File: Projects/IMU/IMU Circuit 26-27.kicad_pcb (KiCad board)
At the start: 2 copper layers, 55 x 75 mm, 20 parts, among them J1 Conn_02x03_Counter_Clockwise, U1 TJA1050DRG, U2 MCP2515-I, U3 TM171, X1 8MHz

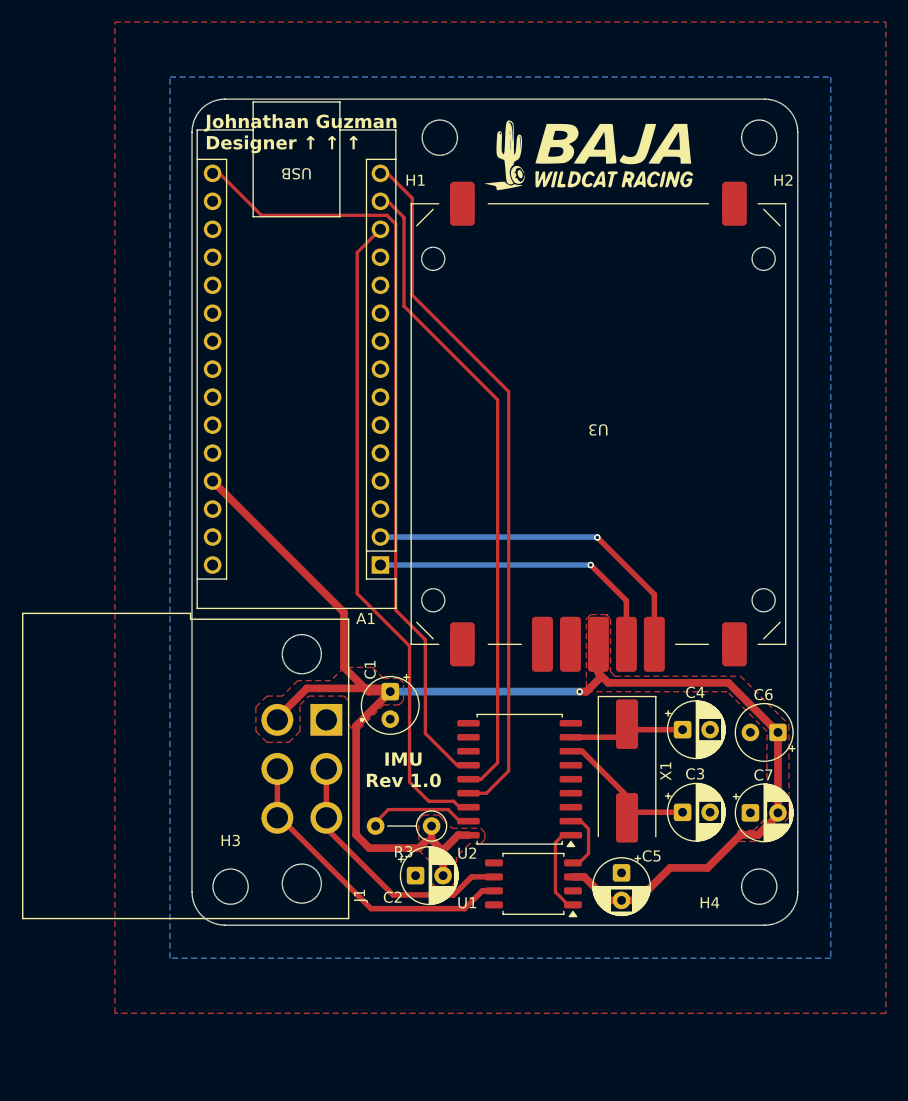
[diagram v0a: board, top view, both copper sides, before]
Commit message: connected int for can controller
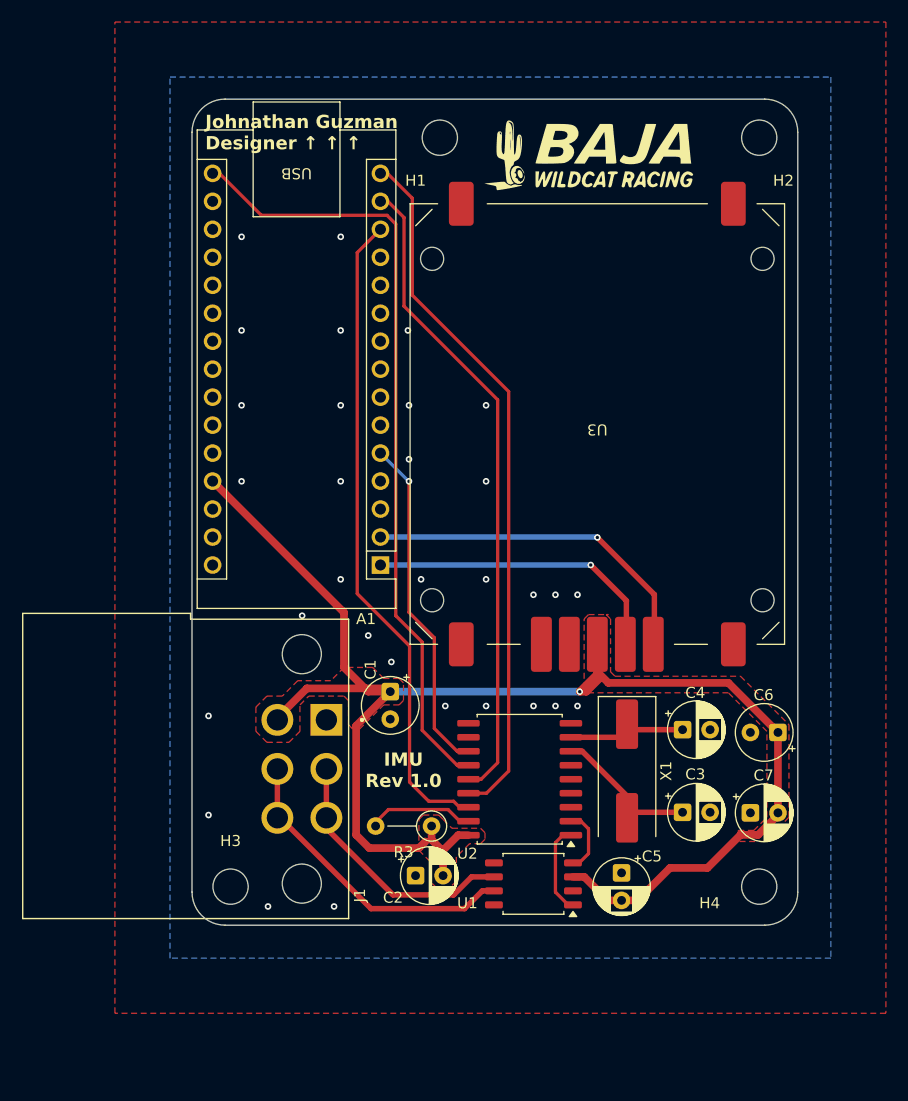
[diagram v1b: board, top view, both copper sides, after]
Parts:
- moved U3 0.10 mm to (138.8, 106.5)
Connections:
- A1 pad 5: unconnected-(A1-D2-Pad5) -> INT
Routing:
- net INT: track 0.00 -> 31.0 mm, vias 0 -> 1
- net +5V: track 138.6 -> 143.5 mm
- net 0: vias 0 -> 31

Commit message: moved some mounting holes
one hole no longer under DTF conn
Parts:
- J1: value Conn_02x03_Counter_Clockwise -> DTF Connector
- moved H3 7.00 mm to (105.5, 155.5)
- moved H4 7.00 mm to (153.5, 155.5)
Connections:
- net 0 renamed GND
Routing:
- net GND: vias 31 -> 29
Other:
- board size 55 x 75 mm -> 55 x 82 mm
- board text added: "BAJA IMU Board Rev 1.0 Designer: Johnathan Guzman"
- board text removed: "IMU Rev 1.0"
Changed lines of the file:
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@@
 			(layers "*.Cu" "*.Mask")
 			(remove_unused_layers no)
-			(net "0")
+			(net "GND")
 			(pinfunction "2_2")
 			(pintype "passive")
@@
 			(layers "F.Cu" "F.Mask" "F.Paste")
 			(roundrect_rratio 0.25)
-			(net "0")
+			(net "GND")
 			(pinfunction "VSS_9")
 			(pintype "passive")
@@
 	(footprint "MountingHole:MountingHole_3.2mm_M3"
 		(layer "F.Cu")
-		(at 105.5 148.5)
+		(at 105.5 155.5)
 		(descr "Mounting Hole 3.2mm, M3, no annular, generated by kicad-footprint-generator mountinghole.py")
 		(tags "mountinghole M3")
@@
 			(layers "*.Cu" "*.Mask")
 			(remove_unused_layers no)
-			(net "0")
+			(net "GND")
 			(pinfunction "2_2")
 			(pintype "passive")
@@
 			(layers "*.Cu" "*.Mask")
 			(remove_unused_layers no)
-			(net "0")
+			(net "GND")
 			(pinfunction "GND_4")
 			(pintype "power_in")
@@
 			(layers "*.Cu" "*.Mask")
 			(remove_unused_layers no)
-			(net "0")
+			(net "GND")
 			(pinfunction "GND_29")
 			(pintype "power_in")
@@
 		)
 		(embedded_fonts no)
-		(model "${KICAD10_3DMODEL_DIR}/Module.3dshapes/Arduino_NANO_CH340.step"
+		(model "${KIPRJMOD}/Arduino_Nano-Rev3.2.stl"
 			(offset
-				(xyz 7.6 -17.8 4)
+				(xyz 0.6 0.8 0)
 			)
 			(scale
@@
 			(layers "*.Cu" "*.Mask")
 			(remove_unused_layers no)
-			(net "0")
+			(net "GND")
 			(pinfunction "2_2")
 			(pintype "passive")
@@
 			)
 		)
-		(property "Value" "Conn_02x03_Counter_Clockwise"
+		(property "Value" "DTF Connector"
 			(at -6.855 -5.795 90)
 			(layer "F.Fab")
@@
 			(layers "*.Cu" "*.Mask")
 			(remove_unused_layers no)
-			(net "0")
+			(net "GND")
 			(pinfunction "Pin_1_1")
 			(pintype "passive")
@@
 			(remove_unused_layers no)
 			(roundrect_rratio 0.15625)
-			(net "0")
+			(net "GND")
 			(pinfunction "1_1")
 			(pintype "passive")
@@
 	(footprint "MountingHole:MountingHole_3.2mm_M3"
 		(layer "F.Cu")
-		(at 153.5 148.5)
+		(at 153.5 155.5)
 		(descr "Mounting Hole 3.2mm, M3, no annular, generated by kicad-footprint-generator mountinghole.py")
 		(tags "mountinghole M3")
@@
 			(layers "F.Cu" "F.Mask" "F.Paste")
 			(roundrect_rratio 0.15)
-			(net "0")
+			(net "GND")
 			(pinfunction "GND_4")
 			(pintype "power_in")
@@
 			(layers "F.Cu" "F.Mask" "F.Paste")
 			(roundrect_rratio 0.15)
-			(net "0")
+			(net "GND")
 			(pinfunction "GND_5")
 			(pintype "power_in")
@@
 			(layers "*.Cu" "*.Mask")
 			(remove_unused_layers no)
-			(net "0")
+			(net "GND")
 			(pinfunction "2_2")
 			(pintype "passive")
@@
 			(layers "F.Cu" "F.Mask" "F.Paste")
 			(roundrect_rratio 0.25)
-			(net "0")
+			(net "GND")
 			(pinfunction "GND_2")
 			(pintype "passive")
@@
 			(layers "F.Cu" "F.Mask" "F.Paste")
 			(roundrect_rratio 0.25)
-			(net "0")
+			(net "GND")
 			(pinfunction "STB_8")
 			(pintype "passive")
@@
 			(remove_unused_layers no)
 			(roundrect_rratio 0.15625)
-			(net "0")
+			(net "GND")
 			(pinfunction "1_1")
 			(pintype "passive")
@@
 			(remove_unused_layers no)
 			(roundrect_rratio 0.15625)
-			(net "0")
+			(net "GND")
 			(pinfunction "1_1")
 			(pintype "passive")
@@
 	)
 	(gr_line
-		(start 102 149)
+		(start 102 156)
 		(end 102 80)
 		(stroke
 			(width 0.05)
-			(type default)
+			(type solid)
 		)
 		(layer "Edge.Cuts")
 	)
 	(gr_arc
-		(start 105 152)
-		(mid 102.87868 151.12132)
-		(end 102 149)
+		(start 105 159)
+		(mid 102.878681 158.121322)
+		(end 102 156.000005)
 		(stroke
 			(width 0.05)
-			(type default)
+			(type solid)
 		)
 		(layer "Edge.Cuts")
@@
 	)
 	(gr_line
-		(start 154 152)
-		(end 105 152)
+		(start 154 159)
+		(end 105 159)
 		(stroke
 			(width 0.05)
-			(type default)
+			(type solid)
 		)
 		(layer "Edge.Cuts")
@@
 	(gr_line
 		(start 157 80)
-		(end 157 149)
+		(end 157 156)
 		(stroke
 			(width 0.05)
-			(type default)
+			(type solid)
 		)
 		(layer "Edge.Cuts")
 	)
 	(gr_arc
-		(start 157 149)
-		(mid 156.12132 151.12132)
-		(end 154 152)
+		(start 157 156)
+		(mid 156.12132 158.12132)
+		(end 154 159)
 		(stroke
 			(width 0.05)
-			(type default)
+			(type solid)
 		)
 		(layer "Edge.Cuts")
@@
 		)
 	)
-	(gr_text "IMU\nRev 1.0"
-		(at 121.2 139.6 0)
+	(gr_text "BAJA IMU Board Rev 1.0\nDesigner: Johnathan Guzman"
+		(at 129.25 156.5 0)
 		(layer "F.SilkS" knockout)
 		(effects
@@
 		(layers "F.Cu" "B.Cu")
 		(free yes)
-		(net "0")
+		(net "GND")
 	)
 	(via
@@
 		(layers "F.Cu" "B.Cu")
 		(free yes)
-		(net "0")
+		(net "GND")
 	)
 	(via
@@
 		(layers "F.Cu" "B.Cu")
 		(free yes)
-		(net "0")
+		(net "GND")
 	)
 	(via
@@
 		(layers "F.Cu" "B.Cu")
 		(free yes)
-		(net "0")
+		(net "GND")
 	)
 	(via
@@
 		(layers "F.Cu" "B.Cu")
 		(free yes)
-		(net "0")
+		(net "GND")
 	)
 	(via
@@
 		(layers "F.Cu" "B.Cu")
 		(free yes)
-		(net "0")
+		(net "GND")
 	)
 	(via
@@
 		(layers "F.Cu" "B.Cu")
 		(free yes)
-		(net "0")
+		(net "GND")
 	)
 	(via
@@
 		(layers "F.Cu" "B.Cu")
 		(free yes)
-		(net "0")
+		(net "GND")
 	)
 	(via
@@
 		(layers "F.Cu" "B.Cu")
 		(free yes)
-		(net "0")
+		(net "GND")
 	)
 	(via
@@
 		(layers "F.Cu" "B.Cu")
 		(free yes)
-		(net "0")
+		(net "GND")
 	)
 	(via
@@
 		(layers "F.Cu" "B.Cu")
 		(free yes)
-		(net "0")
+		(net "GND")
 	)
 	(via
@@
 		(layers "F.Cu" "B.Cu")
 		(free yes)
-		(net "0")
+		(net "GND")
 	)
 	(via
@@
 		(layers "F.Cu" "B.Cu")
 		(free yes)
-		(net "0")
+		(net "GND")
 	)
 	(via
@@
 		(layers "F.Cu" "B.Cu")
 		(free yes)
-		(net "0")
+		(net "GND")
 	)
 	(via
@@
 		(layers "F.Cu" "B.Cu")
 		(free yes)
-		(net "0")
+		(net "GND")
 	)
 	(via
@@
 		(layers "F.Cu" "B.Cu")
 		(free yes)
-		(net "0")
+		(net "GND")
 	)
 	(via
@@
 		(layers "F.Cu" "B.Cu")
 		(free yes)
-		(net "0")
+		(net "GND")
 	)
 	(via
@@
 		(layers "F.Cu" "B.Cu")
 		(free yes)
-		(net "0")
-	)
-	(via
-		(at 135 132.1)
-		(size 0.6)
-		(drill 0.3)
-		(layers "F.Cu" "B.Cu")
-		(free yes)
-		(net "0")
+		(net "GND")
 	)
 	(via
@@
 		(layers "F.Cu" "B.Cu")
 		(free yes)
-		(net "0")
+		(net "GND")
 	)
 	(via
@@
 		(layers "F.Cu" "B.Cu")
 		(free yes)
-		(net "0")
+		(net "GND")
 	)
 	(via
@@
 		(layers "F.Cu" "B.Cu")
 		(free yes)
-		(net "0")
+		(net "GND")
 	)
 	(via
@@
 		(layers "F.Cu" "B.Cu")
 		(free yes)
-		(net "0")
-	)
-	(via
-		(at 135 122)
-		(size 0.6)
-		(drill 0.3)
-		(layers "F.Cu" "B.Cu")
-		(free yes)
-		(net "0")
+		(net "GND")
 	)
 	(via
@@
 		(layers "F.Cu" "B.Cu")
 		(free yes)
-		(net "0")
+		(net "GND")
 	)
 	(via
@@
 		(layers "F.Cu" "B.Cu")
 		(free yes)
-		(net "0")
+		(net "GND")
 	)
 	(via
@@
 		(layers "F.Cu" "B.Cu")
 		(free yes)
-		(net "0")
+		(net "GND")
 	)
 	(via
@@
 		(layers "F.Cu" "B.Cu")
 		(free yes)
-		(net "0")
+		(net "GND")
 	)
 	(via
@@
 		(layers "F.Cu" "B.Cu")
 		(free yes)
-		(net "0")
+		(net "GND")
 	)
 	(via
@@
 		(layers "F.Cu" "B.Cu")
 		(free yes)
-		(net "0")
+		(net "GND")
 	)
 	(via
@@
 		(layers "F.Cu" "B.Cu")
 		(free yes)
-		(net "0")
+		(net "GND")
 	)
 	(segment
@@
 	)
 	(zone
-		(net "0")
+		(net "GND")
 		(layer "F.Cu")
 		(hatch edge 0.5)
@@
 		(polygon
 			(pts
-				(xy 95 70) (xy 165 70) (xy 165 160) (xy 95 160)
+				(xy 95 70) (xy 165 70) (xy 165 166) (xy 95 166)
 			)
 		)
@@
 	)
 	(zone
-		(net "0")
+		(net "GND")
 		(layer "B.Cu")
 		(hatch edge 0.5)
 		(connect_pads
-			(clearance 0.25)
+			(clearance 0.22)
 		)
-		(min_thickness 0.25)
+		(min_thickness 0.22)
 		(fill yes
 			(thermal_gap 0.5)
@@
 		(polygon
 			(pts
-				(xy 100 75) (xy 160 75) (xy 160 155) (xy 100 155)
+				(xy 100 78) (xy 160 78) (xy 160 161) (xy 100 161)
 			)
 		)

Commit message: term R added
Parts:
- added Term Resistor: 120, Resistor_THT:R_Axial_DIN0207_L6.3mm_D2.5mm_P5.08mm_Vertical, F.Cu at (115.0, 153.5)
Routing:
- net High: track 28.2 -> 39.9 mm
- net Low: track 23.8 -> 33.7 mm
- net GND: vias 29 -> 30
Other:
- board text added: "IMU Board Rev 1.0 10/18/26"
- board text added: "Program Here ↑ ↑ ↑ ↑ ↑ ↑ ↑"
- board text removed: "IMU Board Rev 1.0 10/04/26"
- board text removed: "Johnathan Guzman Designer ↑ ↑ ↑"
